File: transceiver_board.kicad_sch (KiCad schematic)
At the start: 7 parts

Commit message: Move key ICs to their own sheet to allow parallel work
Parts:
- removed ADC: AD9288BSTZ-40, ST_48_ADI, symbol local_library:AD9288BSTZ-40
- removed DAC: MAX5180BEEIT, SOP63P602X175-28N, symbol local_library:MAX5180BEEIT
- removed Demodulator: AD8348ARUZ, RU_28_ADI, symbol local_library:AD8348ARUZ
- removed Ethernet_Port: 7499410440, symbol local_library:7499410440
- removed FPGA: Artix-7 Dev Board, symbol local_library:FPGA
- removed Modulator: AD8345AREZ, symbol local_library:AD8345AREZ
- removed PHY_Interface: KSZ8721BT, TQFP48_7x7MC_MCH, symbol local_library:KSZ8721BT
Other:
- added sheet ADC (ADC.kicad_sch)
- added sheet DAC (DAC.kicad_sch)
- added sheet Demodulator (demod.kicad_sch)
- added sheet FPGA (FPGA.kicad_sch)
- added sheet Modulator (mod.kicad_sch)
- added sheet PHY Interface (PHY.kicad_sch)
- added sheet RJ45 (RJ45.kicad_sch)

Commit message: Add Comparator (#1)
* Remove old QAM (de)modulator parts

* Add comparator

* add comparator caps
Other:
- removed sheet ADC
- removed sheet DAC
- removed sheet Demodulator
- removed sheet Modulator
- added sheet Comparator (comparator.kicad_sch)
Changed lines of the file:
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@@
 (kicad_sch (version 20211123) (generator eeschema)
   (paper "A2")
-  (sheet (at 15.24 13.97) (size 142.24 82.55) (fields_autoplaced)
+  (sheet (at 16.51 16.51) (size 185.42 114.3) (fields_autoplaced)
     (stroke (width 0.1524) (type solid) (color 0 0 0 0))
     (fill (color 0 0 0 0.0000))
-    (property "Sheet name" "RJ45" (id 0) (at 15.24 13.2584 0)
+    (property "Sheet name" "RJ45" (id 0) (at 16.51 15.7984 0)
       (effects (font (size 1.27 1.27)) (justify left bottom))
     )
-    (property "Sheet file" "RJ45.kicad_sch" (id 1) (at 15.24 97.1046 0)
+    (property "Sheet file" "RJ45.kicad_sch" (id 1) (at 16.51 131.3946 0)
       (effects (font (size 1.27 1.27)) (justify left top))
     )
   )
-  (sheet (at 430.53 13.97) (size 140.97 82.55) (fields_autoplaced)
+  (sheet (at 16.51 138.43) (size 185.42 105.41) (fields_autoplaced)
     (stroke (width 0.1524) (type solid) (color 0 0 0 0))
     (fill (color 0 0 0 0.0000))
-    (property "Sheet name" "Modulator" (id 0) (at 430.53 13.2584 0)
+    (property "Sheet name" "Comparator" (id 0) (at 16.51 137.7184 0)
       (effects (font (size 1.27 1.27)) (justify left bottom))
     )
-    (property "Sheet file" "mod.kicad_sch" (id 1) (at 430.53 97.1046 0)
+    (property "Sheet file" "comparator.kicad_sch" (id 1) (at 16.51 244.4246 0)
       (effects (font (size 1.27 1.27)) (justify left top))
     )
   )
-  (sheet (at 295.91 13.97) (size 127 82.55) (fields_autoplaced)
+  (sheet (at 208.28 16.51) (size 175.26 114.3) (fields_autoplaced)
     (stroke (width 0.1524) (type solid) (color 0 0 0 0))
     (fill (color 0 0 0 0.0000))
-    (property "Sheet name" "DAC" (id 0) (at 295.91 13.2584 0)
+    (property "Sheet name" "PHY Interface" (id 0) (at 208.28 15.7984 0)
       (effects (font (size 1.27 1.27)) (justify left bottom))
     )
-    (property "Sheet file" "DAC.kicad_sch" (id 1) (at 295.91 97.1046 0)
+    (property "Sheet file" "PHY.kicad_sch" (id 1) (at 208.28 131.3946 0)
       (effects (font (size 1.27 1.27)) (justify left top))
     )
   )
-  (sheet (at 166.37 13.97) (size 119.38 82.55) (fields_autoplaced)
+  (sheet (at 388.62 16.51) (size 187.96 114.3) (fields_autoplaced)
     (stroke (width 0.1524) (type solid) (color 0 0 0 0))
     (fill (color 0 0 0 0.0000))
-    (property "Sheet name" "PHY Interface" (id 0) (at 166.37 13.2584 0)
+    (property "Sheet name" "FPGA" (id 0) (at 388.62 15.7984 0)
       (effects (font (size 1.27 1.27)) (justify left bottom))
     )
-    (property "Sheet file" "PHY.kicad_sch" (id 1) (at 166.37 97.1046 0)
-      (effects (font (size 1.27 1.27)) (justify left top))
-    )
-  )
-  (sheet (at 17.78 111.76) (size 139.7 86.36) (fields_autoplaced)
-    (stroke (width 0.1524) (type solid) (color 0 0 0 0))
-    (fill (color 0 0 0 0.0000))
-    (property "Sheet name" "FPGA" (id 0) (at 17.78 111.0484 0)
-      (effects (font (size 1.27 1.27)) (justify left bottom))
-    )
-    (property "Sheet file" "FPGA.kicad_sch" (id 1) (at 17.78 198.7046 0)
-      (effects (font (size 1.27 1.27)) (justify left top))
-    )
-  )
-  (sheet (at 166.37 111.76) (size 119.38 86.36) (fields_autoplaced)
-    (stroke (width 0.1524) (type solid) (color 0 0 0 0))
-    (fill (color 0 0 0 0.0000))
-    (property "Sheet name" "ADC" (id 0) (at 166.37 111.0484 0)
-      (effects (font (size 1.27 1.27)) (justify left bottom))
-    )
-    (property "Sheet file" "ADC.kicad_sch" (id 1) (at 166.37 198.7046 0)
-      (effects (font (size 1.27 1.27)) (justify left top))
-    )
-  )
-  (sheet (at 295.91 111.76) (size 127 86.36) (fields_autoplaced)
-    (stroke (width 0.1524) (type solid) (color 0 0 0 0))
-    (fill (color 0 0 0 0.0000))
-    (property "Sheet name" "Demodulator" (id 0) (at 295.91 111.0484 0)
-      (effects (font (size 1.27 1.27)) (justify left bottom))
-    )
-    (property "Sheet file" "demod.kicad_sch" (id 1) (at 295.91 198.7046 0)
+    (property "Sheet file" "FPGA.kicad_sch" (id 1) (at 388.62 131.3946 0)
       (effects (font (size 1.27 1.27)) (justify left top))
     )
@@
     (path "/8e682951-d8d0-4614-a72d-99ac2c01b394" (page "3"))
     (path "/9252f6c6-964c-4a99-bc96-7468213f7a97" (page "4"))
-    (path "/ac63a10a-4e4a-4959-a584-16fd62947e00" (page "5"))
-    (path "/89749a37-5722-495e-a4a0-9dc2a298bcdc" (page "6"))
-    (path "/cac37bca-658a-401b-a4cb-03c5dd4f630a" (page "7"))
-    (path "/34da82f0-26e0-4c78-bc7c-b4ced14ddc35" (page "8"))
+    (path "/51bba4f8-4ea3-409a-8f3c-dd75ae3bfb55" (page "5"))
   )
   (symbol_instances
-    (path "/ac63a10a-4e4a-4959-a584-16fd62947e00/ed68ebd5-589f-4017-bc04-9c466a9acf27"
-      (reference "ADC?") (unit 1) (value "AD9288BSTZ-40") (footprint "ST_48_ADI")
+    (path "/51bba4f8-4ea3-409a-8f3c-dd75ae3bfb55/1a8b304b-45e5-49bb-aa50-edadc02513e4"
+      (reference "#PWR?") (unit 1) (value "GND") (footprint "")
     )
-    (path "/89749a37-5722-495e-a4a0-9dc2a298bcdc/c514767f-a4d4-47ac-915f-85487c99d64c"
-      (reference "DAC?") (unit 1) (value "MAX5180BEEIT") (footprint "SOP63P602X175-28N")
+    (path "/51bba4f8-4ea3-409a-8f3c-dd75ae3bfb55/369e047b-679e-446a-81ea-88f02349b84f"
+      (reference "#PWR?") (unit 1) (value "GND") (footprint "")
     )
-    (path "/cac37bca-658a-401b-a4cb-03c5dd4f630a/7b64303d-cb9d-4bff-bb53-d43fbbd5e8a9"
-      (reference "Demodulator?") (unit 1) (value "AD8348ARUZ") (footprint "RU_28_ADI")
+    (path "/51bba4f8-4ea3-409a-8f3c-dd75ae3bfb55/41794cb3-6906-40da-ab23-fac7c0b8a73d"
+      (reference "#PWR?") (unit 1) (value "GND") (footprint "")
+    )
+    (path "/51bba4f8-4ea3-409a-8f3c-dd75ae3bfb55/d9f100e9-02ee-4368-ba05-a9e50ad1330b"
+      (reference "#PWR?") (unit 1) (value "GND") (footprint "")
+    )
+    (path "/51bba4f8-4ea3-409a-8f3c-dd75ae3bfb55/45ac3d35-0e07-40e3-b2f6-1daee7c64de7"
+      (reference "C?") (unit 1) (value "2u2") (footprint "")
+    )
+    (path "/51bba4f8-4ea3-409a-8f3c-dd75ae3bfb55/7a7faf29-9736-40de-9707-4410dc4e29cd"
+      (reference "C?") (unit 1) (value "100n") (footprint "")
+    )
+    (path "/51bba4f8-4ea3-409a-8f3c-dd75ae3bfb55/81a9c681-5a9d-4a87-87dc-c8c3532f3132"
+      (reference "C?") (unit 1) (value "100n") (footprint "")
+    )
+    (path "/51bba4f8-4ea3-409a-8f3c-dd75ae3bfb55/aaa0908f-ac48-4471-a2be-8f6cd57d7370"
+      (reference "C?") (unit 1) (value "100n") (footprint "")
+    )
+    (path "/51bba4f8-4ea3-409a-8f3c-dd75ae3bfb55/e4560c4b-2407-4c44-b528-3ed45367607a"
+      (reference "C?") (unit 1) (value "100n") (footprint "")
+    )
+    (path "/51bba4f8-4ea3-409a-8f3c-dd75ae3bfb55/ecbfb128-2ae5-4031-a519-40fab930e4a6"
+      (reference "C?") (unit 1) (value "2u2") (footprint "")
     )
     (path "/2ed4948e-59e2-4bfe-884a-1c527b3a5f14/916207f4-4bf4-4de8-9a57-0ebee3b5f380"
@@
       (reference "FPGA?") (unit 1) (value "Artix-7 Dev Board") (footprint "")
     )
-    (path "/34da82f0-26e0-4c78-bc7c-b4ced14ddc35/0804e54c-5c84-4925-a937-07358693c834"
-      (reference "Modulator?") (unit 1) (value "AD8345AREZ") (footprint "")
-    )
     (path "/8e682951-d8d0-4614-a72d-99ac2c01b394/e69d0b19-2f64-4d2d-8597-7b71bd218f10"
       (reference "PHY_Interface?") (unit 1) (value "KSZ8721BT") (footprint "TQFP48_7x7MC_MCH")
     )
+    (path "/51bba4f8-4ea3-409a-8f3c-dd75ae3bfb55/7a619027-97df-498d-8a0c-2c78f3c2bc46"
+      (reference "RV?") (unit 1) (value "R_Potentiometer") (footprint "")
+    )
+    (path "/51bba4f8-4ea3-409a-8f3c-dd75ae3bfb55/72b49ec8-c68f-4d04-913b-fe685e96edee"
+      (reference "U?") (unit 1) (value "ltc6752ims8-2-pbf") (footprint "MSOP-8_MS")
+    )
   )

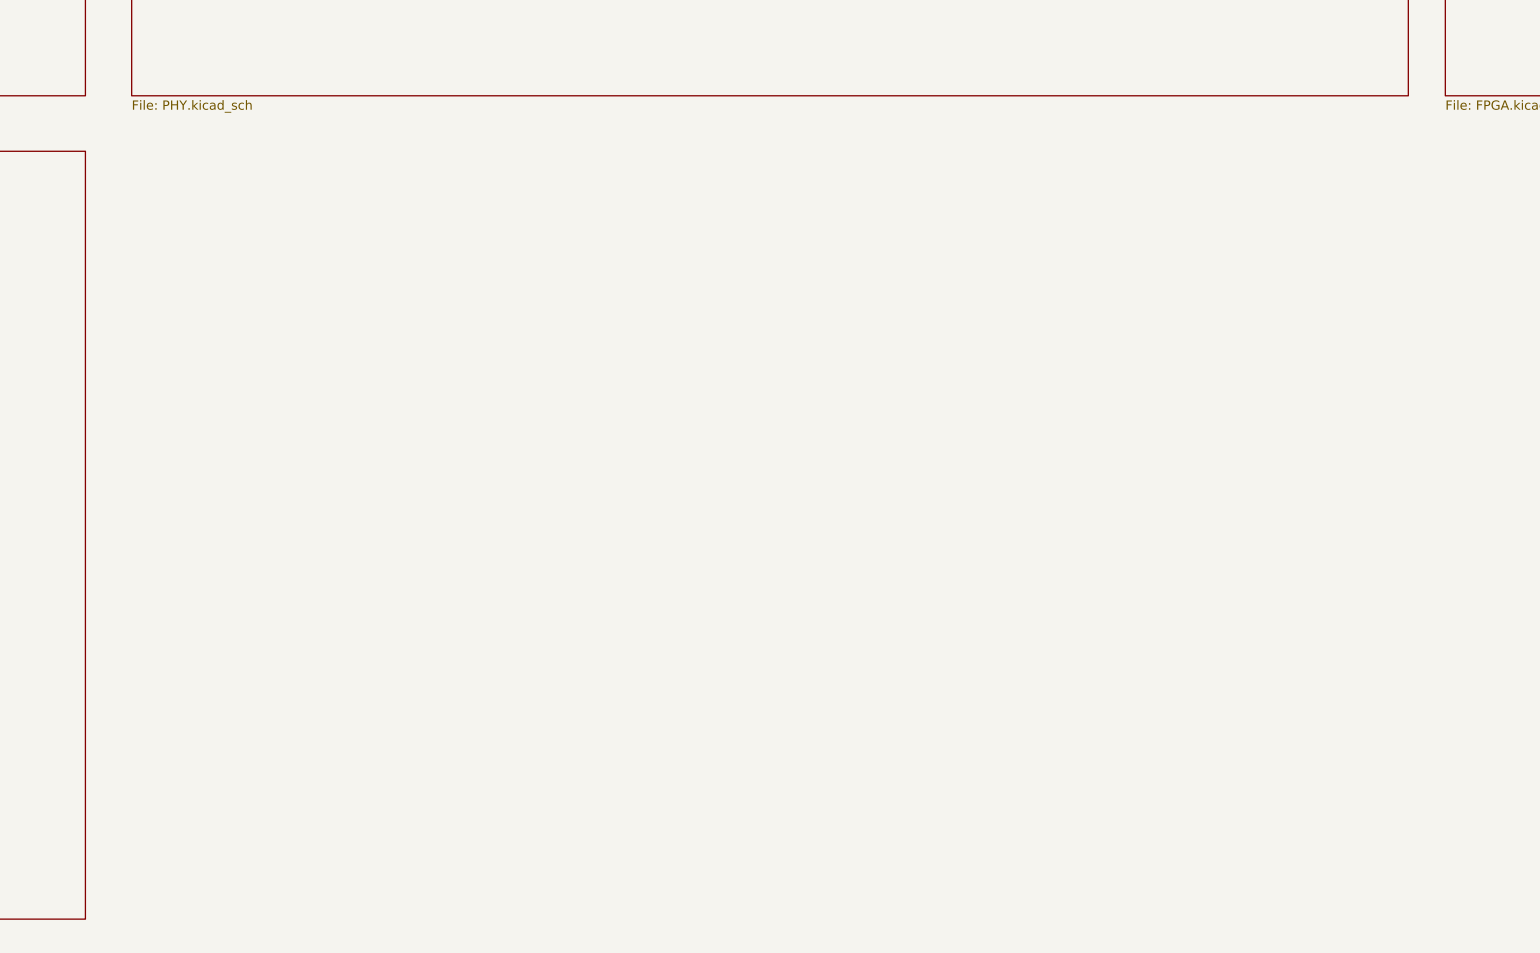
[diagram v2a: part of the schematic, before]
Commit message: Add Heirarchy sheeet for receiver and initial schematic
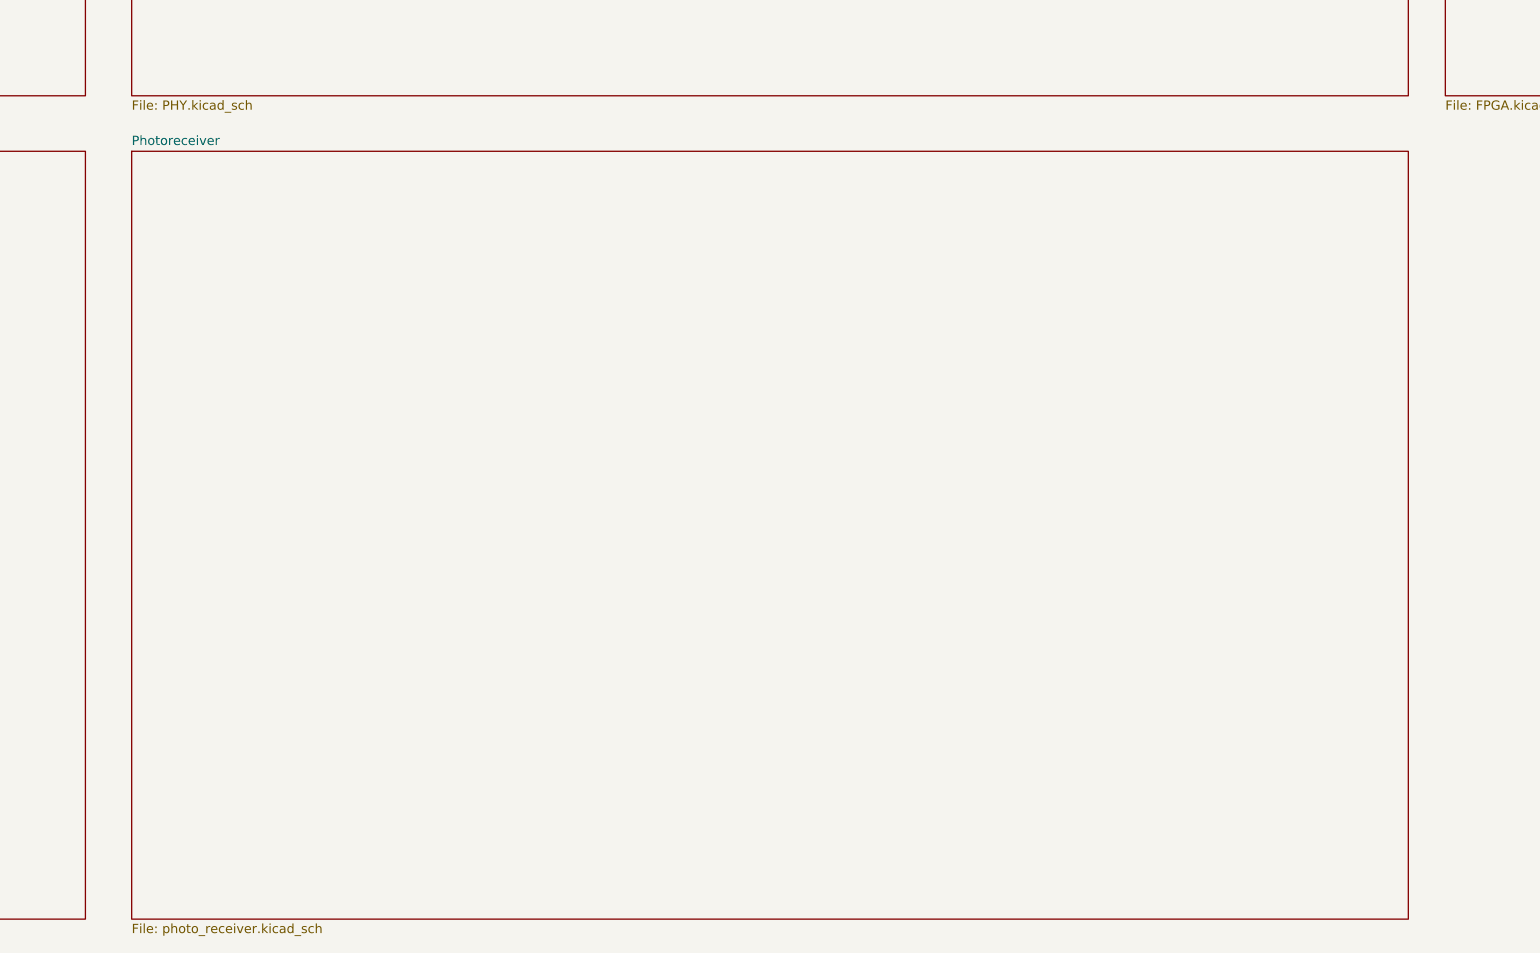
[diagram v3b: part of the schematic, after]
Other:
- added sheet Photoreceiver (photo_receiver.kicad_sch)
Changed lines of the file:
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@@
+    )
+  )
+  (sheet (at 208.28 138.43) (size 175.26 105.41) (fields_autoplaced)
+    (stroke (width 0.1524) (type solid) (color 0 0 0 0))
+    (fill (color 0 0 0 0.0000))
+    (property "Sheet name" "Photoreceiver" (id 0) (at 208.28 137.7184 0)
+      (effects (font (size 1.27 1.27)) (justify left bottom))
+    )
+    (property "Sheet file" "photo_receiver.kicad_sch" (id 1) (at 208.28 244.4246 0)
+      (effects (font (size 1.27 1.27)) (justify left top))
     )
   )
@@
     (path "/9252f6c6-964c-4a99-bc96-7468213f7a97" (page "4"))
     (path "/51bba4f8-4ea3-409a-8f3c-dd75ae3bfb55" (page "5"))
+    (path "/ba74941e-d0cd-46a4-ade7-f1aec57ffafc" (page "6"))
   )
   (symbol_instances
     (path "/51bba4f8-4ea3-409a-8f3c-dd75ae3bfb55/1a8b304b-45e5-49bb-aa50-edadc02513e4"
+      (reference "#PWR?") (unit 1) (value "GND") (footprint "")
+    )
+    (path "/ba74941e-d0cd-46a4-ade7-f1aec57ffafc/35920afe-40d5-4522-b809-581c7052930d"
       (reference "#PWR?") (unit 1) (value "GND") (footprint "")
     )
@@
     (path "/51bba4f8-4ea3-409a-8f3c-dd75ae3bfb55/d9f100e9-02ee-4368-ba05-a9e50ad1330b"
       (reference "#PWR?") (unit 1) (value "GND") (footprint "")
+    )
+    (path "/ba74941e-d0cd-46a4-ade7-f1aec57ffafc/37390626-ae04-4360-9ff8-4cc9e030e613"
+      (reference "C1") (unit 1) (value "0.1u") (footprint "")
     )
     (path "/51bba4f8-4ea3-409a-8f3c-dd75ae3bfb55/45ac3d35-0e07-40e3-b2f6-1daee7c64de7"
@@
       (reference "C?") (unit 1) (value "2u2") (footprint "")
     )
+    (path "/ba74941e-d0cd-46a4-ade7-f1aec57ffafc/775c16ea-275e-4ff0-8988-f47736df60c6"
+      (reference "C_noise") (unit 1) (value "0.1u") (footprint "")
+    )
     (path "/2ed4948e-59e2-4bfe-884a-1c527b3a5f14/916207f4-4bf4-4de8-9a57-0ebee3b5f380"
       (reference "Ethernet_Port?") (unit 1) (value "7499410440") (footprint "")
@@
       (reference "PHY_Interface?") (unit 1) (value "KSZ8721BT") (footprint "TQFP48_7x7MC_MCH")
     )
+    (path "/ba74941e-d0cd-46a4-ade7-f1aec57ffafc/584ec624-a8dc-44ac-8701-d12fd00a4c29"
+      (reference "PhotoReceiver") (unit 1) (value "FDS010") (footprint "")
+    )
+    (path "/ba74941e-d0cd-46a4-ade7-f1aec57ffafc/1996c559-3c89-4ba6-bd00-1cb04a42d3ce"
+      (reference "R1") (unit 1) (value "49.9") (footprint "")
+    )
+    (path "/ba74941e-d0cd-46a4-ade7-f1aec57ffafc/1c29d240-cf64-4dfe-ba89-1399c7aafc8d"
+      (reference "R2") (unit 1) (value "20k") (footprint "")
+    )
+    (path "/ba74941e-d0cd-46a4-ade7-f1aec57ffafc/29ac7234-e707-4fa6-a2bd-bf55acfb7121"
+      (reference "R3") (unit 1) (value "1.74k") (footprint "")
+    )
+    (path "/ba74941e-d0cd-46a4-ade7-f1aec57ffafc/3f5733dd-948b-4ed9-bdf7-60d1bb6942e2"
+      (reference "R4") (unit 1) (value "49.9") (footprint "")
+    )
     (path "/51bba4f8-4ea3-409a-8f3c-dd75ae3bfb55/7a619027-97df-498d-8a0c-2c78f3c2bc46"
       (reference "RV?") (unit 1) (value "R_Potentiometer") (footprint "")
     )
+    (path "/ba74941e-d0cd-46a4-ade7-f1aec57ffafc/7785fef6-61a3-4219-a040-d5622719f832"
+      (reference "R_noise") (unit 1) (value "1k") (footprint "")
+    )
+    (path "/ba74941e-d0cd-46a4-ade7-f1aec57ffafc/05765386-28d4-41c8-8c5a-f440178f690a"
+      (reference "U?") (unit 1) (value "AD8014ARZ") (footprint "SOIC127P600X175-8N")
+    )
     (path "/51bba4f8-4ea3-409a-8f3c-dd75ae3bfb55/72b49ec8-c68f-4d04-913b-fe685e96edee"

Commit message: merge again
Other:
- added sheet Ethernet Magnetics (ethernet magnetics.kicad_sch)
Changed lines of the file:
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@@
+    )
+  )
+  (sheet (at 430.53 111.76) (size 140.97 86.36) (fields_autoplaced)
+    (stroke (width 0.1524) (type solid) (color 0 0 0 0))
+    (fill (color 0 0 0 0.0000))
+    (property "Sheet name" "Ethernet Magnetics" (id 0) (at 430.53 111.0484 0)
+      (effects (font (size 1.27 1.27)) (justify left bottom))
+    )
+    (property "Sheet file" "ethernet magnetics.kicad_sch" (id 1) (at 430.53 198.7046 0)
+      (effects (font (size 1.27 1.27)) (justify left top))
     )
   )
@@
     (path "/51bba4f8-4ea3-409a-8f3c-dd75ae3bfb55" (page "5"))
     (path "/ba74941e-d0cd-46a4-ade7-f1aec57ffafc" (page "6"))
+	(path "/9c91d18d-68d4-4932-8503-e5dad9f3ecb3" (page "7"))
   )
   (symbol_instances
@@
     (path "/51bba4f8-4ea3-409a-8f3c-dd75ae3bfb55/d9f100e9-02ee-4368-ba05-a9e50ad1330b"
       (reference "#PWR?") (unit 1) (value "GND") (footprint "")
+	)
+    (path "/2ed4948e-59e2-4bfe-884a-1c527b3a5f14/5832ccc5-1d48-4ba8-993e-c25897b10601"
+      (reference "#PWR?") (unit 1) (value "GND") (footprint "")
+    )
+    (path "/2ed4948e-59e2-4bfe-884a-1c527b3a5f14/6af55d6d-3aa8-4038-bc12-e09827806386"
+      (reference "#PWR?") (unit 1) (value "GND") (footprint "")
+    )
+    (path "/2ed4948e-59e2-4bfe-884a-1c527b3a5f14/f696f17d-e54a-4708-b516-10835d65e881"
+      (reference "C?") (unit 1) (value "1000pF, 2kV") (footprint "")
     )
     (path "/ba74941e-d0cd-46a4-ade7-f1aec57ffafc/37390626-ae04-4360-9ff8-4cc9e030e613"
@@
       (reference "FPGA?") (unit 1) (value "Artix-7 Dev Board") (footprint "")
     )
+    (path "/2ed4948e-59e2-4bfe-884a-1c527b3a5f14/baa84674-ad20-4613-871a-531aac59e40e"
+      (reference "J?") (unit 1) (value "RJ45_LED_Shielded") (footprint "")
+    )
+    (path "/34da82f0-26e0-4c78-bc7c-b4ced14ddc35/0804e54c-5c84-4925-a937-07358693c834"
+      (reference "Modulator?") (unit 1) (value "AD8345AREZ") (footprint "")
+    )
     (path "/8e682951-d8d0-4614-a72d-99ac2c01b394/e69d0b19-2f64-4d2d-8597-7b71bd218f10"
       (reference "PHY_Interface?") (unit 1) (value "KSZ8721BT") (footprint "TQFP48_7x7MC_MCH")
@@
     (path "/51bba4f8-4ea3-409a-8f3c-dd75ae3bfb55/72b49ec8-c68f-4d04-913b-fe685e96edee"
       (reference "U?") (unit 1) (value "ltc6752ims8-2-pbf") (footprint "MSOP-8_MS")
+	)
+    (path "/2ed4948e-59e2-4bfe-884a-1c527b3a5f14/061c147f-e231-4c5f-a5cf-5533ead6a90f"
+      (reference "R?") (unit 1) (value "75R") (footprint "")
+    )
+    (path "/9c91d18d-68d4-4932-8503-e5dad9f3ecb3/0d6d225b-c7ca-4091-8ff4-7280ae3d4c01"
+      (reference "R?") (unit 1) (value "75R") (footprint "")
+    )
+    (path "/2ed4948e-59e2-4bfe-884a-1c527b3a5f14/17cd2aad-5960-42d0-a49b-ffbd8e59d997"
+      (reference "R?") (unit 1) (value "75R") (footprint "")
+    )
+    (path "/9c91d18d-68d4-4932-8503-e5dad9f3ecb3/b77bd3ad-3d23-49c9-9edb-17259af96359"
+      (reference "R?") (unit 1) (value "75R") (footprint "")
+    )
+	(path "/51bba4f8-4ea3-409a-8f3c-dd75ae3bfb55/7a619027-97df-498d-8a0c-2c78f3c2bc46"
+      (reference "RV?") (unit 1) (value "R_Potentiometer") (footprint "")
+    )
+    (path "/9c91d18d-68d4-4932-8503-e5dad9f3ecb3/0e48a565-d68b-4f9f-a0c5-a860ed343575"
+      (reference "U?") (unit 1) (value "ALANS10001-4J41ET") (footprint "")
     )
   )
